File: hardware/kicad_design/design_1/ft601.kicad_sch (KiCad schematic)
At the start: 42 parts, among them IC1 MIC7221YM5-TR, J15 USB_C_Receptacle, U2 FT601Q-B-T, U3 HD3SS3212IRKSR, Y1 30Meg

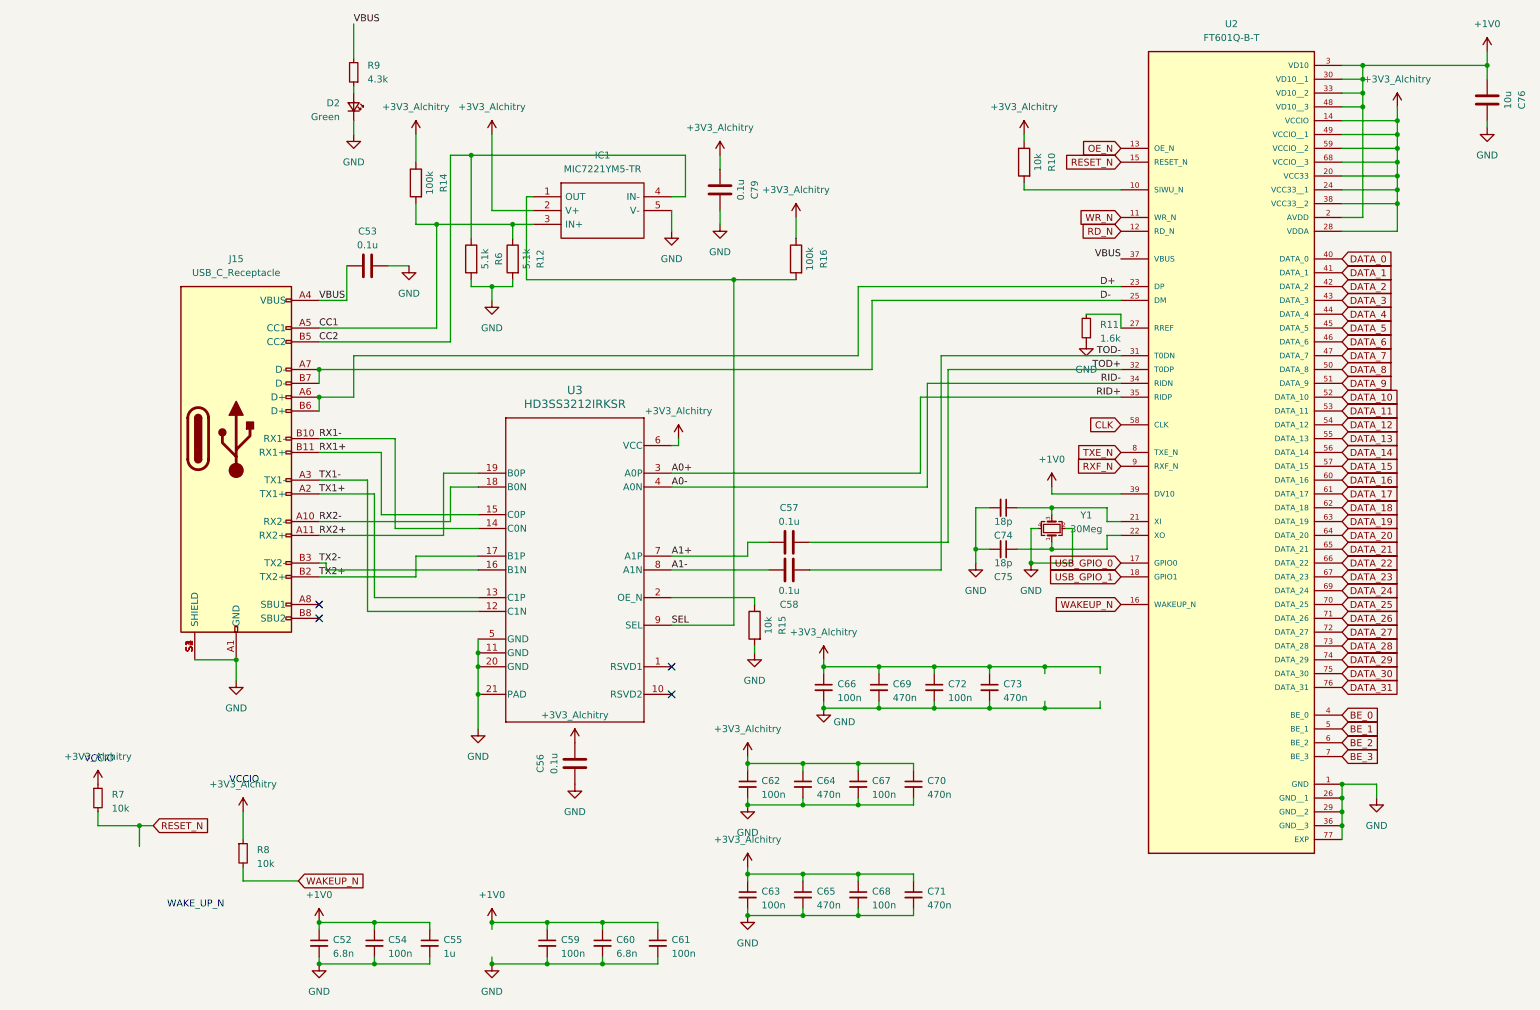
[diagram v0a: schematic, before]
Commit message: rev 5 board with termination resistors, through hole usb c, and minor fixes
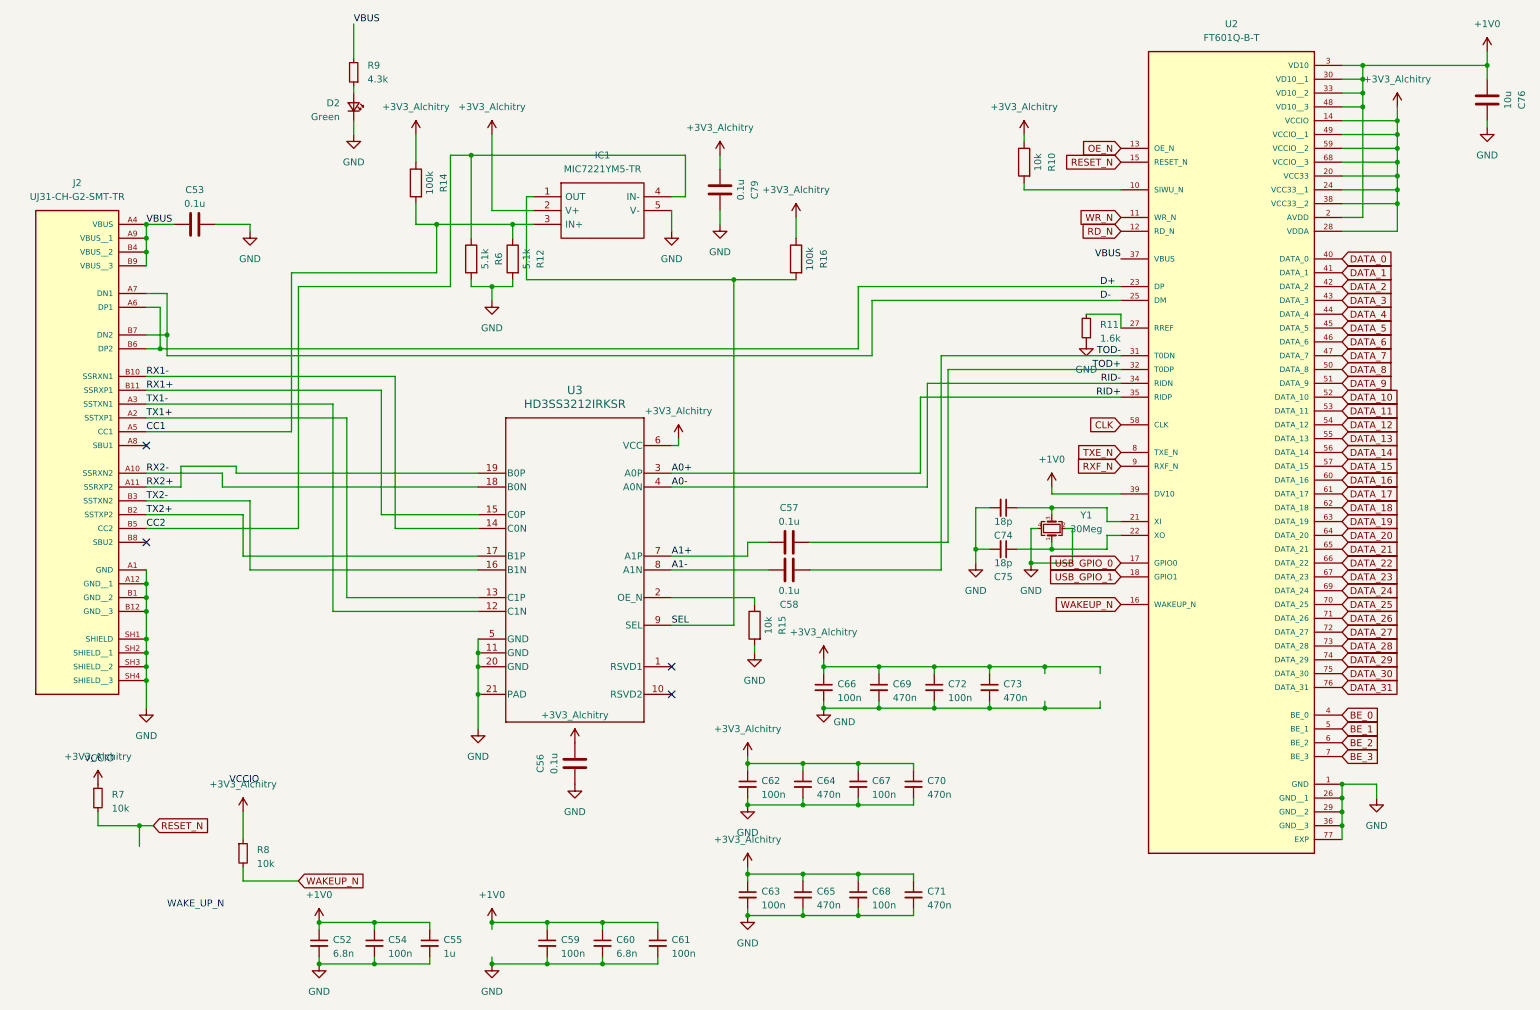
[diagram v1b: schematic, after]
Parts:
- removed J15: USB_C_Receptacle, handheld_mri_footprints:AMPHENOL_12401899E412A, symbol Connector:USB_C_Receptacle
- added J2: UJ31-CH-G2-SMT-TR, handheld_mri_footprints:CUI_UJ31-CH-G2-SMT-TR, symbol Handheld_MRI:UJ31-CH-G2-SMT-TR
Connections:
- net CC1: now also J2.A5 (CC1)
- net CC2: now also J2.B5 (CC2)
- net D+: now also J2.A6 (DP1), J2.B6 (DP2)
- net D-: now also J2.A7 (DN1), J2.B7 (DN2)
- net GND: now also J2.A1 (GND), J2.A12 (GND__1), J2.B1 (GND__2), J2.B12 (GND__3), J2.SH1 (SHIELD), J2.SH2 (SHIELD__1), J2.SH3 (SHIELD__2), J2.SH4 (SHIELD__3)
- net RX1+: now also J2.B11 (SSRXP1)
- net RX1-: now also J2.B10 (SSRXN1)
- net RX2+: now also J2.A11 (SSRXP2)
- net RX2-: now also J2.A10 (SSRXN2)
- net TX1+: now also J2.A2 (SSTXP1)
- net TX1-: now also J2.A3 (SSTXN1)
- net TX2+: now also J2.B2 (SSTXP2)
- net TX2-: now also J2.B3 (SSTXN2)
- net VBUS: now also J2.A4 (VBUS), J2.A9 (VBUS__1), J2.B4 (VBUS__2), J2.B9 (VBUS__3)
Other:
- moved on the sheet: C53
